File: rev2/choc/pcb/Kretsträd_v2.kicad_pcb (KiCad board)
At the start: 2 copper layers, 103.4 x 89.4 mm, 50 parts, among them J1 Conn_01x02_Female, J2 Conn_01x02_Female, J3 Conn_01x02_Female, J4 Conn_01x02_Female, SW1 SW1, SW10 SW10, SW11 SW11, SW12 SW12, SW13 SW13, SW14 SW14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

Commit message: v2.1: pre-production iteration
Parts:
- removed Breakaway1, Breakaway2: Breakaway, jw_custom_footprint:Breakaway_Tabs_1x05_0.3mm
- removed the J1 at (173.0, 112.6)
- removed the J2 at (173.0, 112.6)
- added J3: Conn_01x01_Socket, jw_custom_footprints:Pogopin_socket_1x01_1.00mm_vertical, F.Cu at (94.6, 115.0)
- added J4: Conn_01x01_Socket, jw_custom_footprints:Pogopin_socket_1x01_1.00mm_vertical, F.Cu at (95.7, 123.4)
- D1, D10, D11, D12, D13, D14, D15, D16, D17, D2, D3, D4, D5, D6, D7, D8, D9: footprint jw_custom_footprint:Diode_SOD123_THT_2 -> jw_custom_footprints:Diode_SOD123_THT_2
- SW1, SW10, SW11, SW12, SW13, SW14, SW15, SW16, SW17, SW2, SW3, SW4, SW5, SW6, SW7, SW8, SW9: footprint jw_custom_footprint:Kailh_Choc_PG1350_Hotswap_reversible -> jw_custom_footprints:Kailh_Choc_PG1350_v1+2_Hotswap_reversible
- U1: value SeeeduinoXIAO -> SeeeduinoXIAO_nRF52840; footprint jw_custom_footprints:Xiao THT jumper pad_big_hole_flipped -> jw_custom_footprints:Xiao_nRF52840_THT_jumper_1.55mm_hole
- moved PWR_SW_1 32.0 mm to (148.2, 128.8), turned to -7.5 degrees
- moved PWR_SW_2 32.0 mm to (148.2, 128.8), turned to 172.5 degrees
- moved D16 5.07 mm to (154.9, 111.6)
- moved D2 4.80 mm to (116.3, 61.8)
- moved D12 4.00 mm to (116.3, 96.9)
- moved D7 3.94 mm to (116.3, 80.0)
- moved D6 3.78 mm to (97.8, 83.0)
- moved D11 3.67 mm to (97.8, 100.2)
- moved D13 3.65 mm to (134.2, 94.2)
- moved D8 3.63 mm to (134.2, 77.3)
- moved D3 3.47 mm to (134.2, 60.5)
- moved D1 3.45 mm to (97.8, 61.9), turned to 90 degrees
- moved D17 3.20 mm to (157.8, 122.4)
- moved D5 2.99 mm to (155.5, 62.9), turned to 90 degrees
- moved D10 2.79 mm to (170.5, 87.6)
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- renumbered J3 to J1, J4 to J2
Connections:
- PWR_SW_1 pad 1: unconnected-(PWR_SW_1-A-Pad1) -> BAT
- PWR_SW_1 pad 3: RAW -> unconnected-(PWR_SW_1-C-Pad3)
- PWR_SW_2 pad 3: RAW -> BAT
- U1 pad 1: row2 -> row0
- U1 pad 12: VCC -> GND
- U1 pad 13: GND -> unconnected-(U1-5V-Pad13)
- U1 pad 2: row0 -> row1
- U1 pad 3: row1 -> col0
- U1 pad 4: col0 -> col4
- U1 pad 5: col4 -> col3
- U1 pad 6: col3 -> col1
- U1 pad 7: col1 -> row3
- U1 pad 8: row3 -> col2
- U1 pad 9: col2 -> unconnected-(U1-P1.14/A9_D9/MISO-Pad9)_1
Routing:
- net RAW: track 124.6 -> 0.00 mm, vias 3 -> 0
- net BAT: track 0.00 -> 95.7 mm, vias 0 -> 2
- net row0: track 152.8 -> 138.4 mm, vias 3 -> 1
- net col3: track 167.2 -> 153.8 mm, vias 10 -> 7
- net BT+: track 39.3 -> 28.4 mm, vias 3 -> 2
- net col0: track 84.5 -> 94.5 mm
- net Net-(D16-A): track 18.1 -> 8.61 mm, vias 2 -> 0
- net row2: track 105.0 -> 114.4 mm
- net unconnected-(U1-3V3-Pad11): track 9.32 -> 0.00 mm, vias 1 -> 0
- net unconnected-(U1-PA5_A9_D9_MISO-Pad10): track 9.31 -> 0.00 mm, vias 1 -> 0
- net VCC: track 9.26 -> 0.00 mm, vias 1 -> 0
- net row1: track 132.6 -> 136.8 mm, vias 3 -> 1
- net col4: track 159.2 -> 162.8 mm, vias 9 -> 8
- net Net-(D11-A): track 13.5 -> 10.0 mm
- net Net-(D6-A): track 13.5 -> 10.2 mm
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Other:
- board size 103.4 x 89.4 mm -> 104.9 x 89.8 mm
- board text added: "Kretsträd v2.1 PCB by jw"
- board text removed: "Kretsträd v2 Designed by jw"

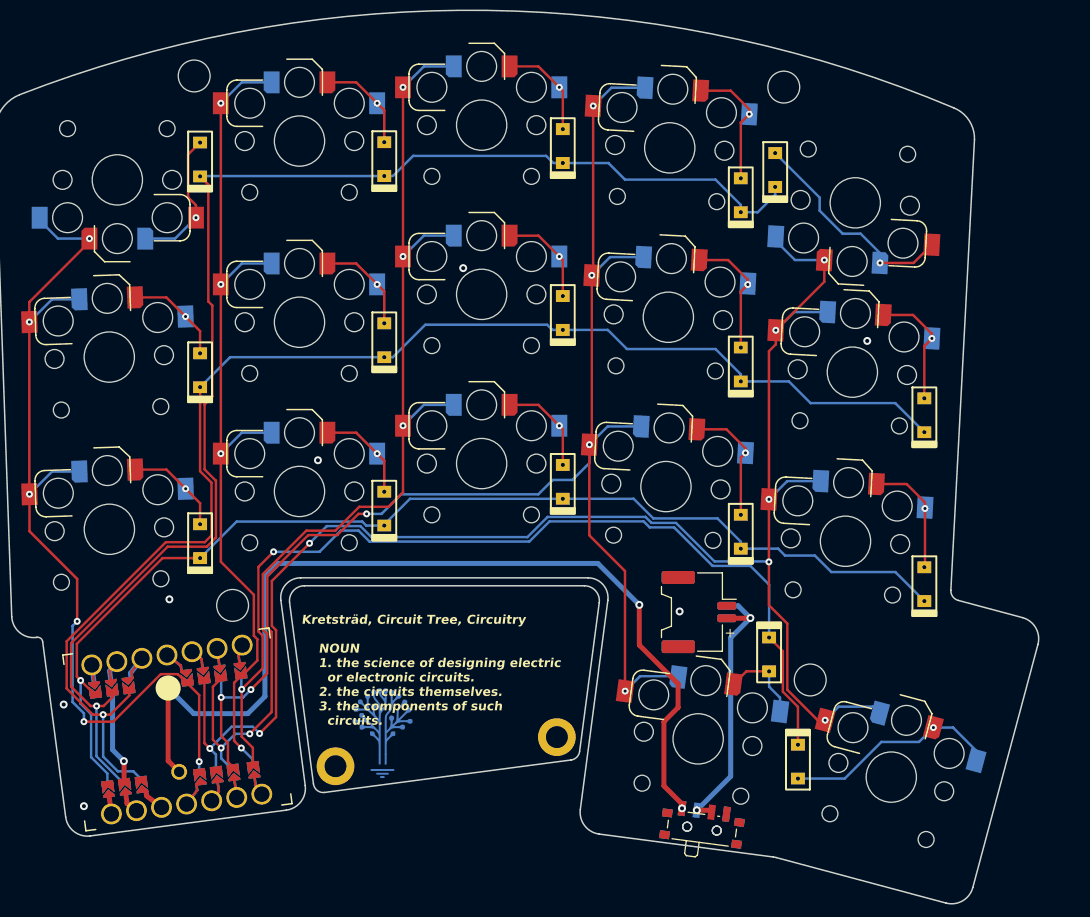
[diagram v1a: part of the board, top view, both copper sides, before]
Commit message: v2: pre-production: added supplementary power switches; tweaks here and there
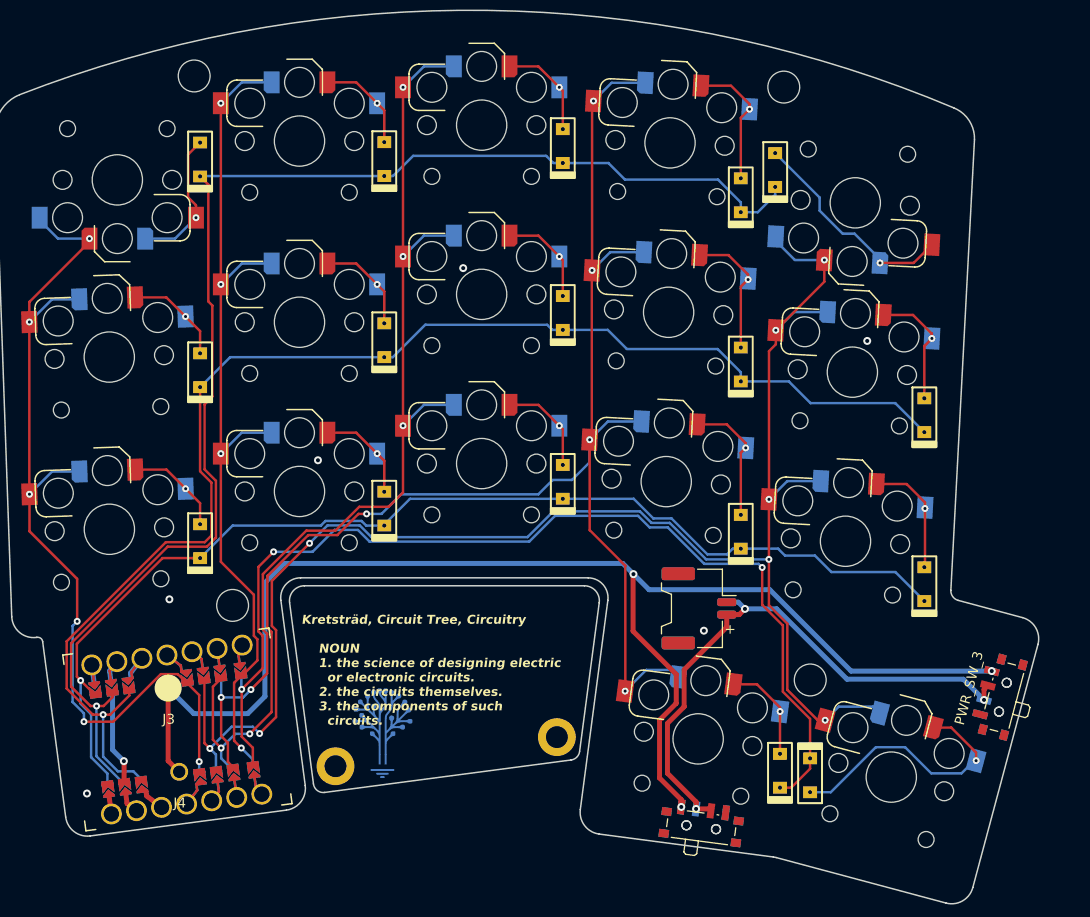
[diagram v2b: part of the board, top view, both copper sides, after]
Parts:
- added PWR_SW_3: SW_SPDT, Button_Switch_SMD:SW_SPDT_PCM12, F.Cu at (178.1, 115.8)
- added PWR_SW_4: SW_SPDT, Button_Switch_SMD:SW_SPDT_PCM12, B.Cu at (178.1, 115.8)
- J3, J4: footprint jw_custom_footprints:Pogopin_socket_1x01_1.00mm_vertical -> jw_custom_footprints:Pogopin_socket_1x01_1.20mm_vertical
- moved D16 11.7 mm to (156.0, 123.3), turned to 90 degrees
- moved D17 1.84 mm to (159.0, 123.7)
- moved SW14 0.50 mm to (144.6, 94.2)
- moved SW4 0.50 mm to (145.0, 60.2)
- moved SW9 0.50 mm to (144.8, 77.2)
- moved J1 0.37 mm to (147.9, 107.0)
- moved J2 0.37 mm to (147.9, 107.0)
- moved PWR_SW_1 0.16 mm to (148.1, 128.6)
- moved PWR_SW_2 0.16 mm to (148.1, 128.6)
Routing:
- net BAT: track 95.7 -> 136.9 mm, vias 2 -> 3
- net BT+: track 28.4 -> 58.3 mm, vias 2 -> 3
- net row3: track 96.7 -> 104.5 mm, vias 2 -> 3
- net Net-(D17-A): track 22.0 -> 26.3 mm
- net Net-(D16-A): track 8.61 -> 10.3 mm, vias 0 -> 1
- net col3: track 153.8 -> 154.9 mm
- net Net-(D4-A): track 13.0 -> 13.5 mm
- net Net-(D9-A): track 12.8 -> 13.3 mm
- net Net-(D14-A): track 12.5 -> 13.1 mm
- net GND: vias 8 -> 7

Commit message: v2.1: first production
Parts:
- moved TH2 1.11 mm to (157.2, 55.3)
- moved D4 1.00 mm to (153.1, 65.5)
- moved SW4 1.00 mm to (146.0, 60.2)
- moved SW5 0.80 mm to (164.4, 66.3)
- moved D5 0.80 mm to (156.3, 63.0)
- moved D10 0.76 mm to (171.1, 88.0)
- moved D9 0.70 mm to (152.8, 82.5)
- moved SW9 0.70 mm to (145.5, 77.2)
- moved D14 0.50 mm to (152.6, 99.3)
- moved SW14 0.50 mm to (145.1, 94.2)
- moved D15 0.50 mm to (171.0, 104.5)
- moved SW10 0.50 mm to (163.8, 83.2)
- moved SW15 0.50 mm to (163.1, 100.2)
- moved TH3 0.34 mm to (100.7, 106.5)
- moved TH1 0.20 mm to (97.0, 53.5)
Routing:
- net col3: track 154.9 -> 156.5 mm
- net col4: track 163.2 -> 164.4 mm
- net row1: track 137.0 -> 138.2 mm
- net row3: track 104.5 -> 105.4 mm
- net col2: track 101.4 -> 102.0 mm
- net GND: vias 7 -> 6
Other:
- board size 104.9 x 89.8 mm -> 104.9 x 89.6 mm

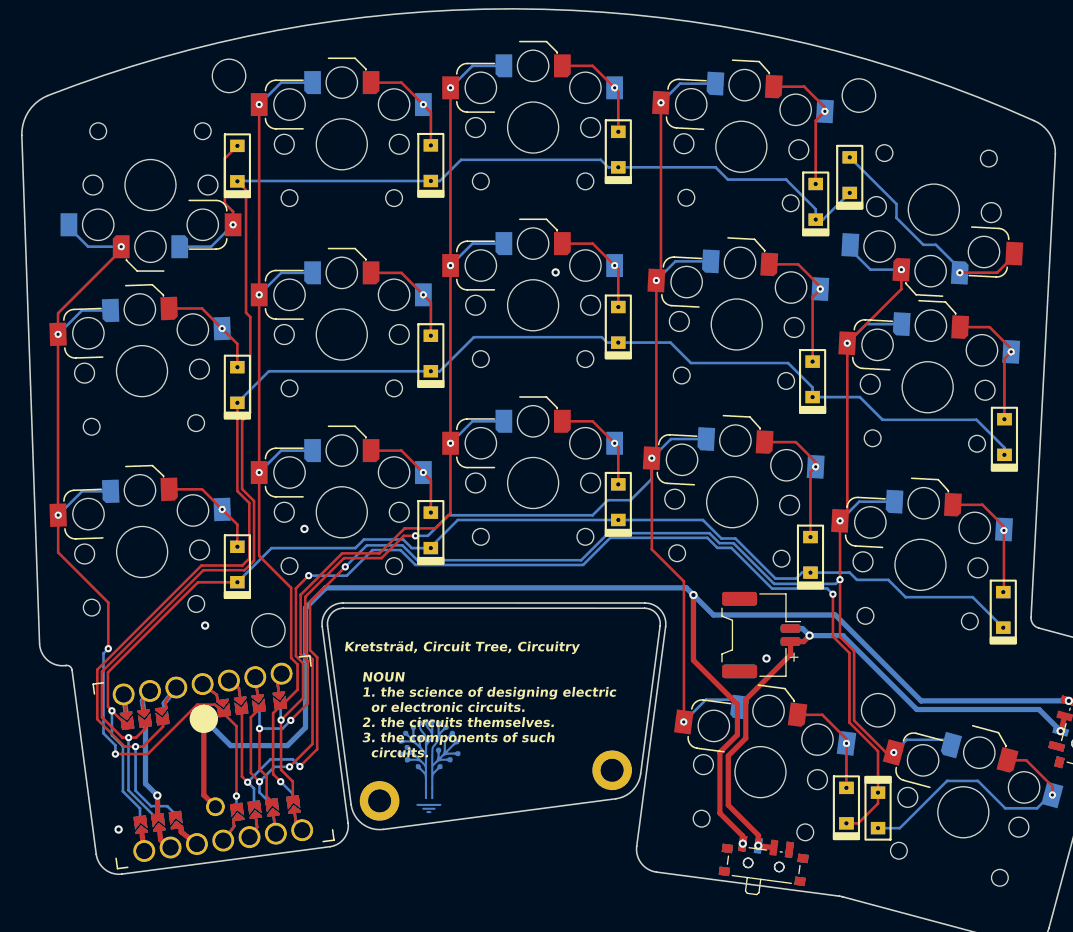
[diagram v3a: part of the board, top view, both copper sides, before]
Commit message: v2: Modified v2 pcb, built stack-style case
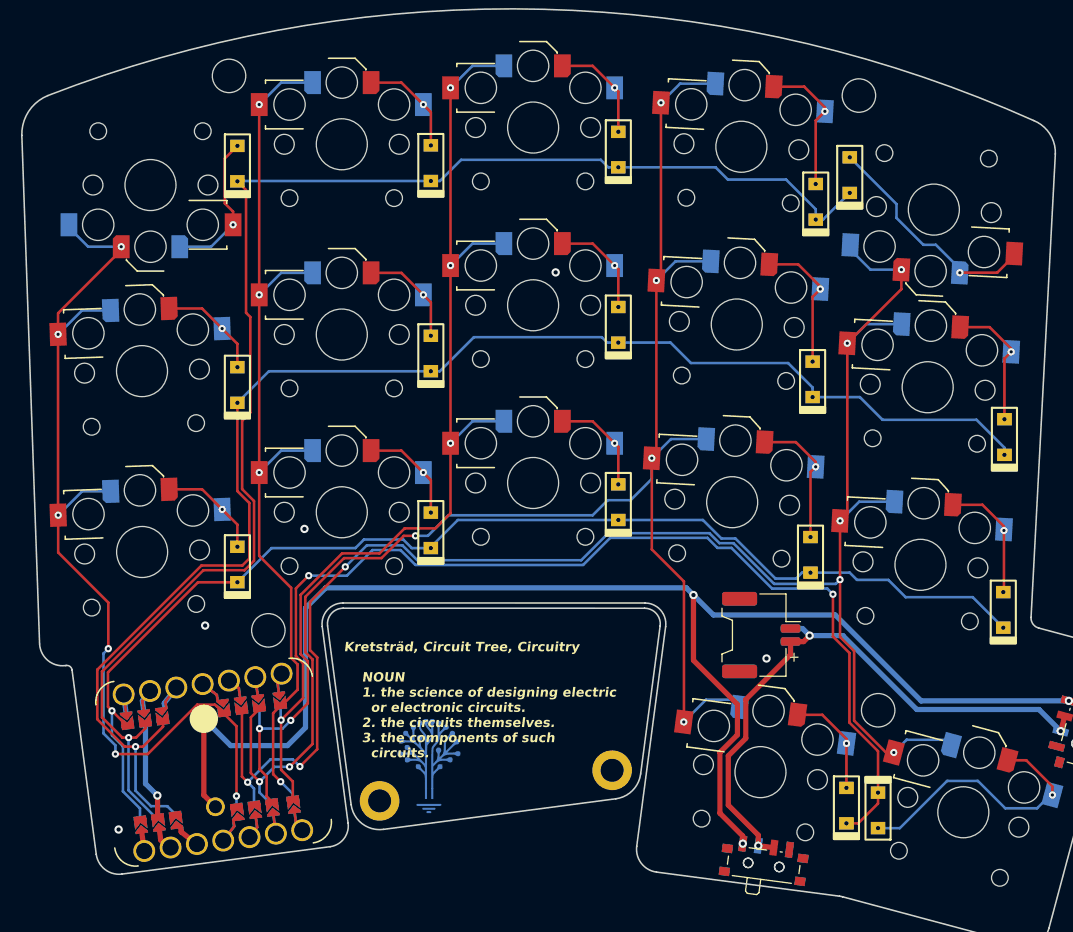
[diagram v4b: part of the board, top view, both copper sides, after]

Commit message: v2.2
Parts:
- removed the PWR_SW_1 at (148.1, 128.6)
- removed the PWR_SW_2 at (148.1, 128.6)
- added PWR_SW_3: SW_DPDT, jw_custom_footprints:Button_Switch_Push_Vertical_2P2T_Toggle_5.8x5.8, F.Cu at (175.2, 112.3)
- added PWR_SW_4: SW_DPDT, jw_custom_footprints:Button_Switch_Push_Horizontal_2P2T_Toggle_5.8x5.8, F.Cu at (175.7, 111.7)
- D1, D10, D11, D12, D13, D14, D15, D16, D17, D2, D3, D4, D5, D6, D7, D8, D9: footprint jw_custom_footprints:Diode_SOD123_THT_2 -> jw_custom_footprints:Diode_SOD123_THT_v3
- moved PWR_SW_1 33.8 mm to (146.7, 128.5), turned to -7.5 degrees
- moved PWR_SW_2 33.8 mm to (146.7, 128.5), turned to 172.5 degrees
- moved D2 0.55 mm to (116.3, 62.4)
- moved SW2 0.55 mm to (107.7, 60.6)
- moved D1 0.50 mm to (97.8, 62.4)
- moved D6 0.31 mm to (97.5, 83.0)
- moved SW6 0.31 mm to (88.3, 81.7)
- moved TH3 0.30 mm to (100.7, 106.2)
- moved SW15 0.10 mm to (163.0, 100.2)
- renumbered PWR_SW_3 to PWR_SW_1, PWR_SW_4 to PWR_SW_2
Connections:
- PWR_SW_1 pad 1: unconnected-(PWR_SW_3-A-Pad1) -> BAT
- PWR_SW_1 pad 3: BAT -> unconnected-(PWR_SW_1-C-Pad3)
- PWR_SW_2 pad 1: BAT -> unconnected-(PWR_SW_2-A-Pad1)
- PWR_SW_2 pad 3: unconnected-(PWR_SW_4-C-Pad3) -> BAT
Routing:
- net col1: track 87.8 -> 115.2 mm, vias 4 -> 6
- net BT+: track 58.1 -> 64.3 mm, vias 3 -> 2
- net row0: track 138.9 -> 144.6 mm, vias 1 -> 2
- net row1: track 138.2 -> 141.8 mm, vias 1 -> 2
- net GND: track 9.27 -> 5.87 mm, vias 6 -> 10
- net row3: track 105.4 -> 108.5 mm
- net col3: track 156.5 -> 154.1 mm
- net col2: track 102.0 -> 100.2 mm
- net BAT: track 137.2 -> 138.9 mm, vias 3 -> 2
- net row2: track 114.5 -> 113.0 mm
- net col4: track 164.4 -> 165.1 mm
- net col0: vias 6 -> 5
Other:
- board size 104.9 x 89.6 mm -> 104.7 x 89.6 mm
- board text added: "Cirque Trackpad TM023023"
- board text added: "Cirque Trackpad TM035035"
- board text added: "Kretsträd v2.2 PCB by jw"
- board text added: "Xxxx-xxxx"
- board text removed: "Kretsträd v2.1 PCB by jw"
